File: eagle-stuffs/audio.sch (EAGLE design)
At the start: 30 parts, among them IC1 SSM2211SZ, IC2 TL084P, IC3 DS1804-50k, IC4 DS1804-10k

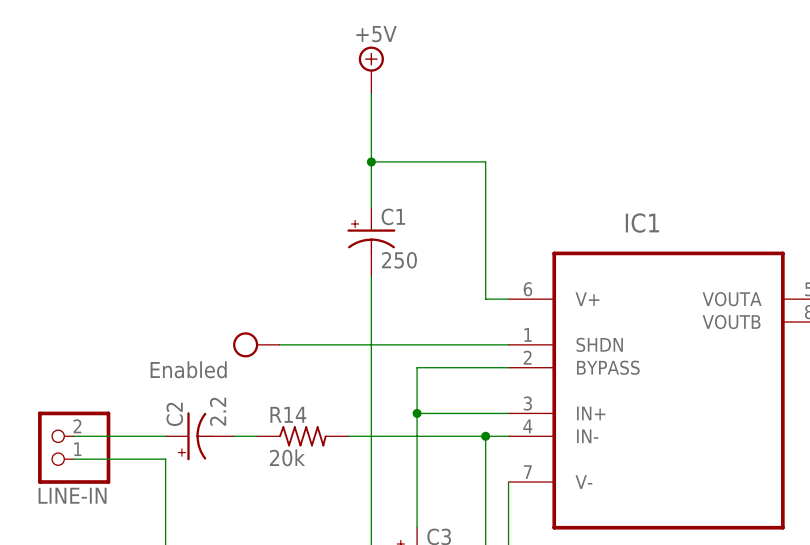
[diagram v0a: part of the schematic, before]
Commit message: C1 value changed
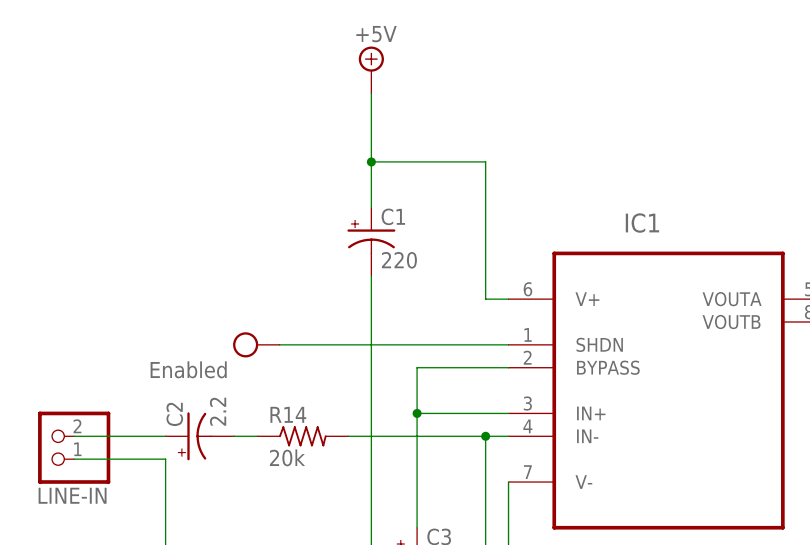
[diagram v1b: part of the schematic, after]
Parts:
- C1: value 250 -> 220
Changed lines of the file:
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@@
 <part name="R13" library="rcl" deviceset="R-US_" device="0204/2V" value="5.1k"/>
 <part name="R9" library="rcl" deviceset="R-US_" device="0204/2V" value="1k"/>
-<part name="C1" library="rcl" deviceset="CPOL-US" device="E3.5-10" value="250"/>
+<part name="C1" library="rcl" deviceset="CPOL-US" device="E3.5-10" value="220"/>
 <part name="C2" library="rcl" deviceset="CPOL-US" device="E3.5-8" value="2.2"/>
 <part name="C3" library="rcl" deviceset="CPOL-US" device="E3.5-8" value="2.2"/>

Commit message: Added some more info
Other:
- note added: "Buffer"
- note added: "Envelope follower"
- note added: "Preamp"
- note added: "Schmitt Trigger"
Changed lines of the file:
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@@
 <text x="175.26" y="7.62" size="2.54" layer="98" font="fixed">Licensed under CERN OHL v.1.2 or later</text>
 <text x="264.16" y="7.62" size="2.54" layer="98" font="fixed">A</text>
+<text x="76.2" y="45.72" size="1.778" layer="98" font="fixed">Preamp</text>
+<text x="132.08" y="45.72" size="1.778" layer="98" font="fixed">Envelope follower</text>
+<text x="190.5" y="45.72" size="1.778" layer="98" font="fixed">Buffer</text>
+<text x="226.06" y="45.72" size="1.778" layer="98" font="fixed">Schmitt Trigger</text>
 </plain>
 <instances>

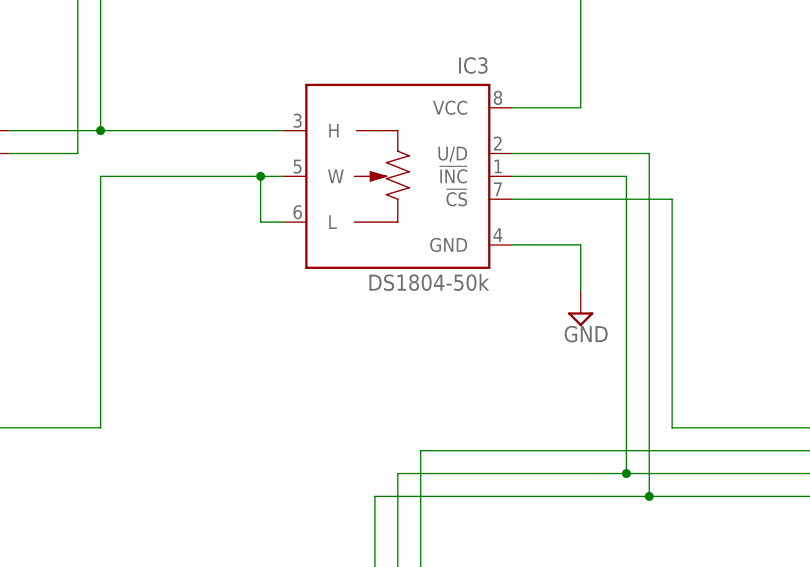
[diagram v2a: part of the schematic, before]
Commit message: adjusted value of digital pot
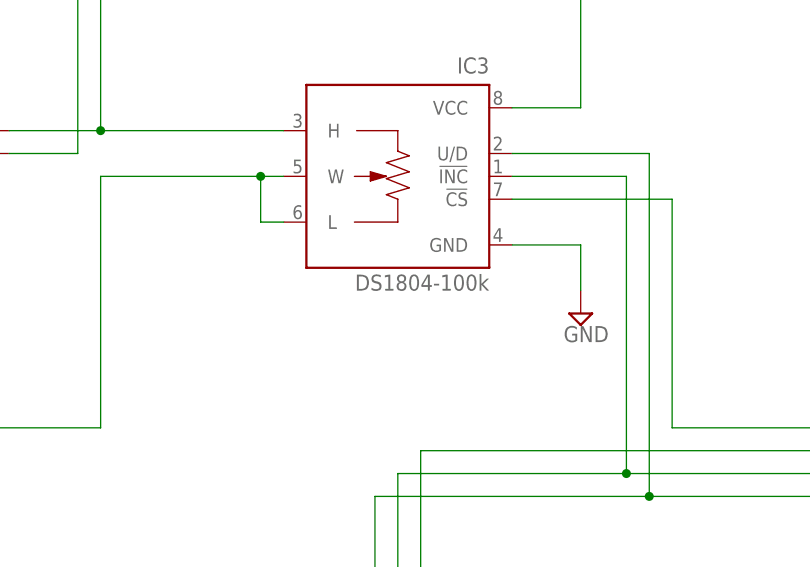
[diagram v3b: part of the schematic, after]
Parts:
- IC3: value DS1804-50k -> DS1804-100k
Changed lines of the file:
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@@
 <part name="FRAME1" library="frames" deviceset="FRAME_A_L" device=""/>
 <part name="IC2" library="linear" deviceset="TL084" device="P"/>
-<part name="IC3" library="pot-xicor" deviceset="X9C102*" device="P" value="DS1804-50k"/>
+<part name="IC3" library="pot-xicor" deviceset="X9C102*" device="P" value="DS1804-100k"/>
 <part name="IC4" library="pot-xicor" deviceset="X9C102*" device="P" value="DS1804-10k"/>
 <part name="SUPPLY1" library="supply2" deviceset="+5V" device=""/>

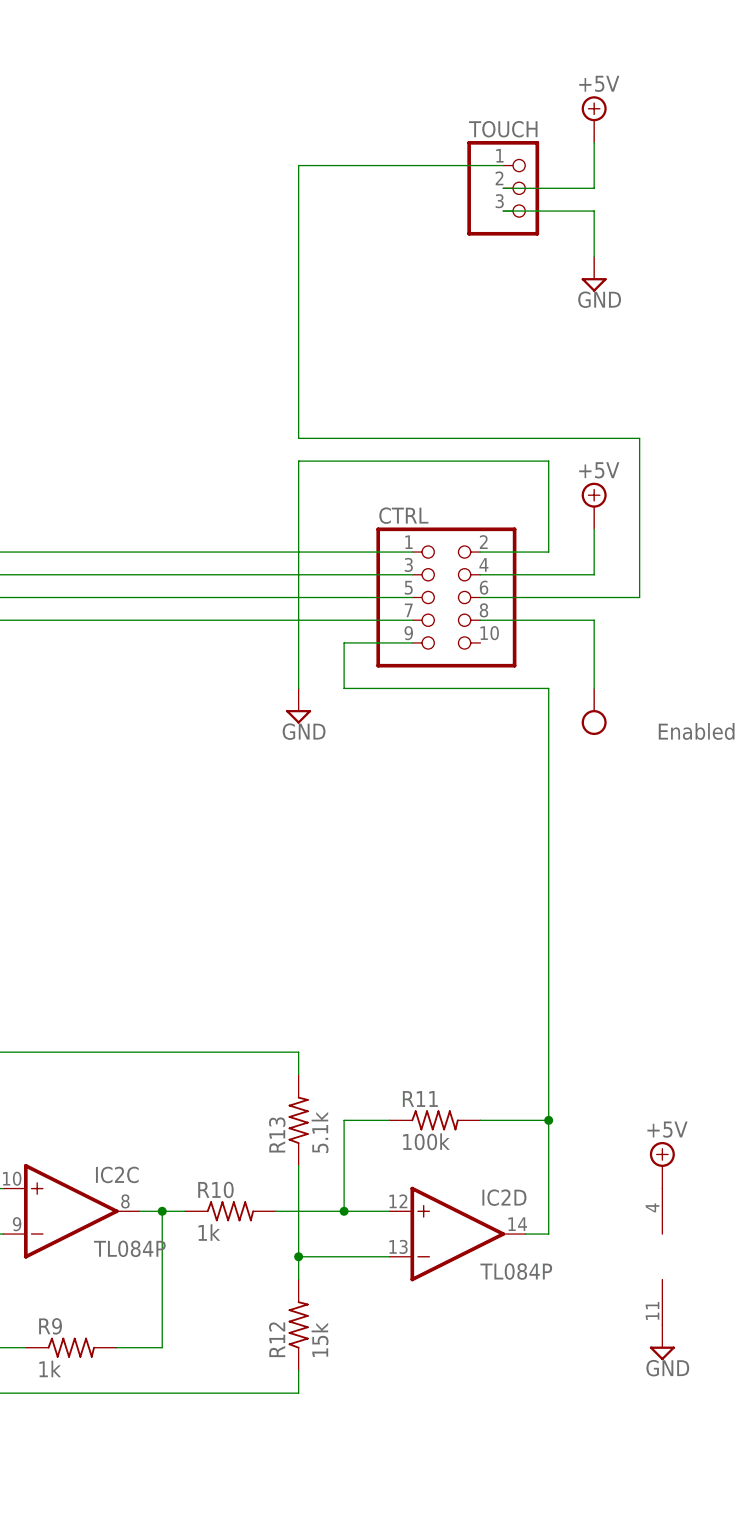
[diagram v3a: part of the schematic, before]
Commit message: Added voltage divider on output
I forgot I was dealing with 3.3v input chip! :-(
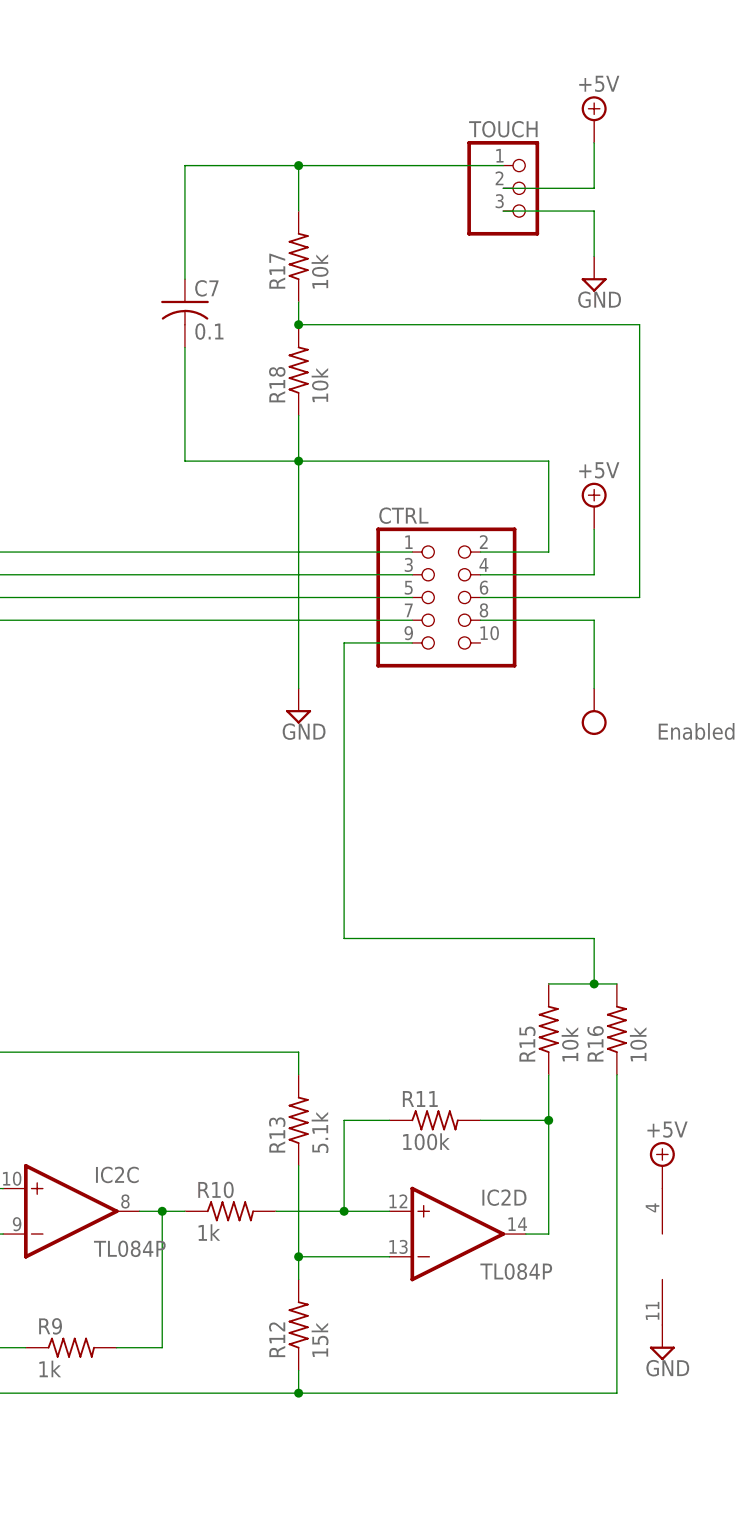
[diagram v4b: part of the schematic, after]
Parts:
- added C7: 0.1, rcl:C-US025-024X044
- added R15, R16, R17, R18: 10k, rcl:R-US_0204/2V
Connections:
- removed net N$22: CTRL.6, TOUCH.1
- new net N$14: IC2D.OUT, R11.2, R15.1
- new net N$16: CTRL.9, R15.2, R16.2
- new net N$30: CTRL.6, R17.1, R18.2
- net GND: now also C7.2, R16.1, R18.1
- net N$28: now also C7.1, R17.2, TOUCH.1; no longer CTRL.9, IC2D.OUT, R11.2
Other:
- note added: "B"
- note removed: "A"
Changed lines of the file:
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@@
 <part name="C2" library="rcl" deviceset="CPOL-US" device="E3.5-8" value="2.2"/>
 <part name="C3" library="rcl" deviceset="CPOL-US" device="E3.5-8" value="2.2"/>
+<part name="R15" library="rcl" deviceset="R-US_" device="0204/2V" value="10k"/>
+<part name="R16" library="rcl" deviceset="R-US_" device="0204/2V" value="10k"/>
+<part name="R17" library="rcl" deviceset="R-US_" device="0204/2V" value="10k"/>
+<part name="R18" library="rcl" deviceset="R-US_" device="0204/2V" value="10k"/>
+<part name="C7" library="rcl" deviceset="C-US" device="025-024X044" value="0.1"/>
 </parts>
 <sheets>
@@
 <text x="193.04" y="25.4" size="2.54" layer="98" font="fixed">Y.A.N.C. (Yet Another Nixie Clock)</text>
 <text x="175.26" y="7.62" size="2.54" layer="98" font="fixed">Licensed under CERN OHL v.1.2 or later</text>
-<text x="264.16" y="7.62" size="2.54" layer="98" font="fixed">A</text>
+<text x="264.16" y="7.62" size="2.54" layer="98" font="fixed">B</text>
 <text x="76.2" y="45.72" size="1.778" layer="98" font="fixed">Preamp</text>
 <text x="132.08" y="45.72" size="1.778" layer="98" font="fixed">Envelope follower</text>
@@
 <instance part="C2" gate="G$1" x="35.56" y="162.56" rot="R90"/>
 <instance part="C3" gate="G$1" x="60.96" y="149.86"/>
+<instance part="R15" gate="G$1" x="248.92" y="91.44" rot="R90"/>
+<instance part="R16" gate="G$1" x="256.54" y="91.44" rot="R90"/>
+<instance part="R17" gate="G$1" x="220.98" y="177.8" rot="R90"/>
+<instance part="R18" gate="G$1" x="220.98" y="165.1" rot="R90"/>
+<instance part="C7" gate="G$1" x="208.28" y="172.72"/>
 </instances>
 <busses>
@@
 <pinref part="R8" gate="G$1" pin="1"/>
 <pinref part="R12" gate="G$1" pin="1"/>
+<pinref part="R16" gate="G$1" pin="1"/>
+<wire x1="220.98" y1="50.8" x2="256.54" y2="50.8" width="0.1524" layer="91"/>
+<wire x1="256.54" y1="50.8" x2="256.54" y2="86.36" width="0.1524" layer="91"/>
+<junction x="220.98" y="50.8"/>
 </segment>
 <segment>
@@
 <wire x1="248.92" y1="154.94" x2="220.98" y2="154.94" width="0.1524" layer="91"/>
 <wire x1="220.98" y1="154.94" x2="220.98" y2="129.54" width="0.1524" layer="91"/>
+<pinref part="R18" gate="G$1" pin="1"/>
+<wire x1="220.98" y1="160.02" x2="220.98" y2="154.94" width="0.1524" layer="91"/>
+<junction x="220.98" y="154.94"/>
+<pinref part="C7" gate="G$1" pin="2"/>
+<wire x1="220.98" y1="154.94" x2="208.28" y2="154.94" width="0.1524" layer="91"/>
+<wire x1="208.28" y1="154.94" x2="208.28" y2="167.64" width="0.1524" layer="91"/>
 </segment>
 </net>
@@
 </segment>
 </net>
-<net name="N$22" class="0">
-<segment>
-<pinref part="CTRL" gate="A" pin="6"/>
-<wire x1="241.3" y1="139.7" x2="259.08" y2="139.7" width="0.1524" layer="91"/>
-<wire x1="259.08" y1="139.7" x2="259.08" y2="157.48" width="0.1524" layer="91"/>
-<wire x1="259.08" y1="157.48" x2="220.98" y2="157.48" width="0.1524" layer="91"/>
-<wire x1="220.98" y1="157.48" x2="220.98" y2="187.96" width="0.1524" layer="91"/>
-<pinref part="TOUCH" gate="A" pin="1"/>
-<wire x1="220.98" y1="187.96" x2="243.84" y2="187.96" width="0.1524" layer="91"/>
-</segment>
-</net>
 <net name="N$8" class="0">
 <segment>
@@
 </segment>
 </net>
-<net name="N$28" class="0">
-<segment>
-<wire x1="241.3" y1="81.28" x2="248.92" y2="81.28" width="0.1524" layer="91"/>
-<wire x1="248.92" y1="81.28" x2="248.92" y2="68.58" width="0.1524" layer="91"/>
-<pinref part="IC2" gate="D" pin="OUT"/>
-<wire x1="248.92" y1="68.58" x2="246.38" y2="68.58" width="0.1524" layer="91"/>
-<pinref part="CTRL" gate="A" pin="9"/>
-<wire x1="233.68" y1="134.62" x2="226.06" y2="134.62" width="0.1524" layer="91"/>
-<wire x1="226.06" y1="134.62" x2="226.06" y2="129.54" width="0.1524" layer="91"/>
-<wire x1="226.06" y1="129.54" x2="248.92" y2="129.54" width="0.1524" layer="91"/>
-<wire x1="248.92" y1="129.54" x2="248.92" y2="81.28" width="0.1524" layer="91"/>
-<junction x="248.92" y="81.28"/>
-<pinref part="R11" gate="G$1" pin="2"/>
-</segment>
-</net>
 <net name="N$29" class="0">
 <segment>
@@
 </segment>
 </net>
+<net name="N$14" class="0">
+<segment>
+<pinref part="IC2" gate="D" pin="OUT"/>
+<pinref part="R11" gate="G$1" pin="2"/>
+<wire x1="241.3" y1="81.28" x2="248.92" y2="81.28" width="0.1524" layer="91"/>
+<wire x1="248.92" y1="81.28" x2="248.92" y2="68.58" width="0.1524" layer="91"/>
+<wire x1="248.92" y1="68.58" x2="246.38" y2="68.58" width="0.1524" layer="91"/>
+<pinref part="R15" gate="G$1" pin="1"/>
+<wire x1="248.92" y1="81.28" x2="248.92" y2="86.36" width="0.1524" layer="91"/>
+<junction x="248.92" y="81.28"/>
+</segment>
+</net>
+<net name="N$16" class="0">
+<segment>
+<pinref part="R16" gate="G$1" pin="2"/>
+<pinref part="R15" gate="G$1" pin="2"/>
+<wire x1="256.54" y1="96.52" x2="254" y2="96.52" width="0.1524" layer="91"/>
+<pinref part="CTRL" gate="A" pin="9"/>
+<wire x1="254" y1="96.52" x2="248.92" y2="96.52" width="0.1524" layer="91"/>
+<wire x1="233.68" y1="134.62" x2="226.06" y2="134.62" width="0.1524" layer="91"/>
+<wire x1="226.06" y1="134.62" x2="226.06" y2="101.6" width="0.1524" layer="91"/>
+<wire x1="226.06" y1="101.6" x2="254" y2="101.6" width="0.1524" layer="91"/>
+<wire x1="254" y1="101.6" x2="254" y2="96.52" width="0.1524" layer="91"/>
+<junction x="254" y="96.52"/>
+</segment>
+</net>
+<net name="N$28" class="0">
+<segment>
+<pinref part="TOUCH" gate="A" pin="1"/>
+<wire x1="220.98" y1="187.96" x2="243.84" y2="187.96" width="0.1524" layer="91"/>
+<pinref part="R17" gate="G$1" pin="2"/>
+<wire x1="220.98" y1="187.96" x2="220.98" y2="182.88" width="0.1524" layer="91"/>
+<pinref part="C7" gate="G$1" pin="1"/>
+<wire x1="220.98" y1="187.96" x2="208.28" y2="187.96" width="0.1524" layer="91"/>
+<wire x1="208.28" y1="187.96" x2="208.28" y2="175.26" width="0.1524" layer="91"/>
+<junction x="220.98" y="187.96"/>
+</segment>
+</net>
+<net name="N$30" class="0">
+<segment>
+<pinref part="R17" gate="G$1" pin="1"/>
+<pinref part="R18" gate="G$1" pin="2"/>
+<wire x1="220.98" y1="172.72" x2="220.98" y2="170.18" width="0.1524" layer="91"/>
+<pinref part="CTRL" gate="A" pin="6"/>
+<wire x1="241.3" y1="139.7" x2="259.08" y2="139.7" width="0.1524" layer="91"/>
+<wire x1="259.08" y1="139.7" x2="259.08" y2="170.18" width="0.1524" layer="91"/>
+<wire x1="220.98" y1="170.18" x2="259.08" y2="170.18" width="0.1524" layer="91"/>
+<junction x="220.98" y="170.18"/>
+</segment>
+</net>
